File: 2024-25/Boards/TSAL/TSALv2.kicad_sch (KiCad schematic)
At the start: 29 parts, among them J1 043045-0412, Q1 DMP2035U-7, Q3 UJ3N065080K3S, Q4 DMN2056U, U1 H11L1M, U2 NE555D

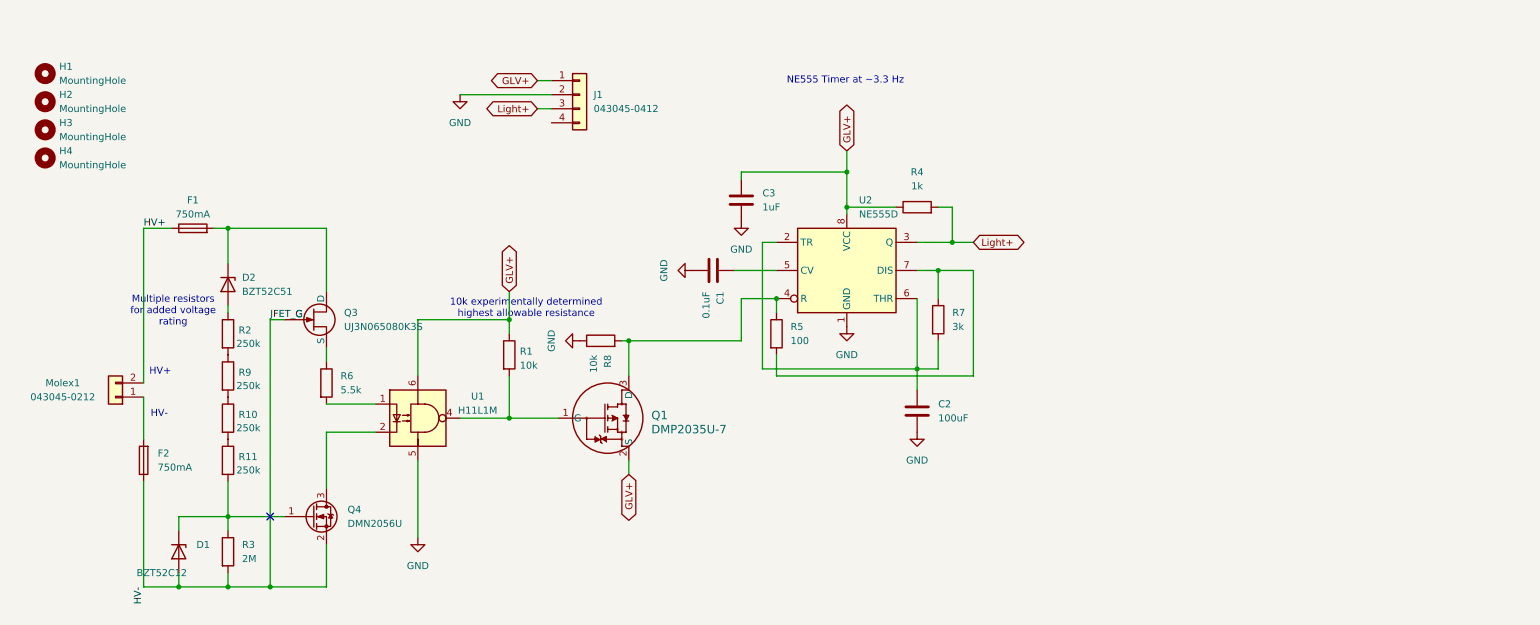
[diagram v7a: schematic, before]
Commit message: fixed up part names and added dnps
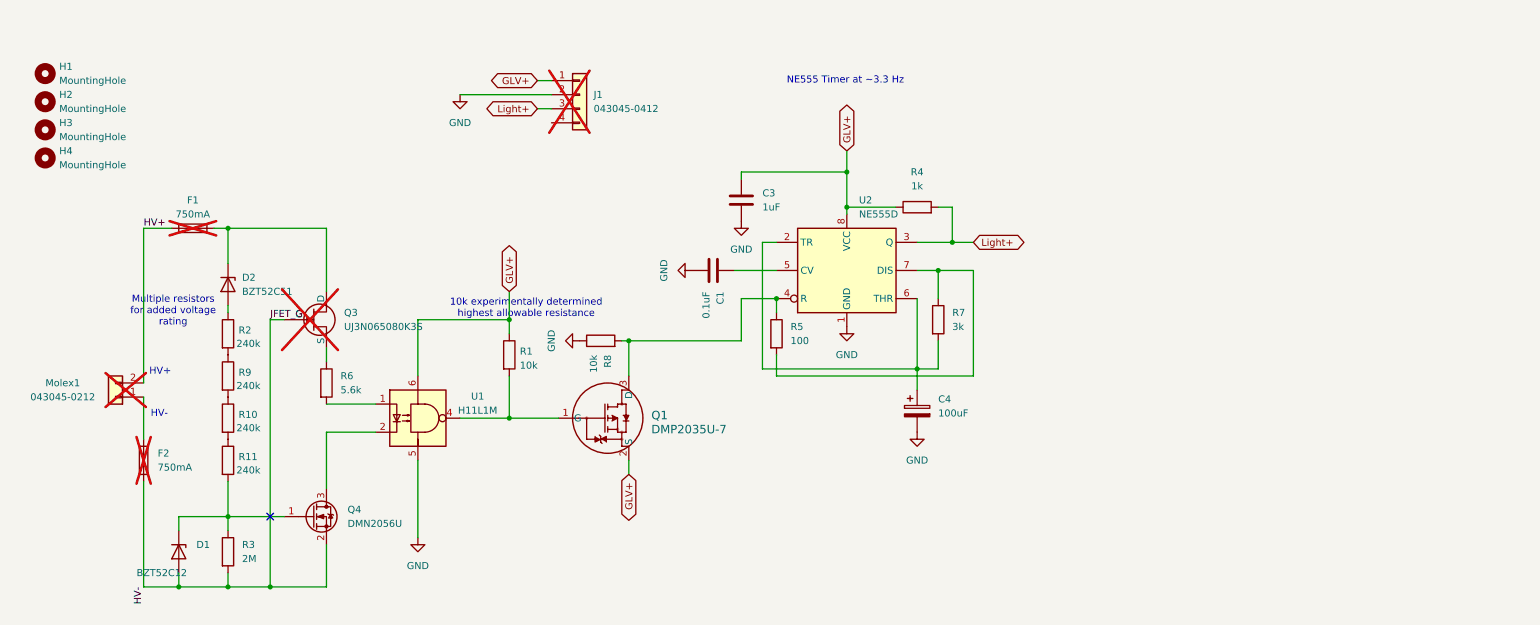
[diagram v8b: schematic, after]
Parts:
- removed C2: 100uF, Capacitor_SMD:C_0805_2012Metric_Pad1.18x1.45mm_HandSolder, symbol Device:C
- added C4: 100uF, Capacitor_SMD:CP_Elec_6.3x5.4, symbol Device:C_Polarized
- F1, F2, J1, Molex1, Q3: now not fitted
- R10, R11, R2, R9: value 250k -> 240k
- R6: value 5.5k -> 5.6k
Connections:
- net GND: now also C4.2
- net at R7.2, U2.2 (TR), U2.6 (THR): now also C4.1
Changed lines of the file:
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@@
 			)
 		)
-		(property "Value" "5.5k"
+		(property "Value" "5.6k"
 			(at 72.39 81.2799 0)
 			(effects
@@
 			)
 		)
-		(property "Value" "250k"
+		(property "Value" "240k"
 			(at 53.594 72.898 0)
 			(effects
@@
 		(in_bom yes)
 		(on_board yes)
-		(dnp no)
+		(dnp yes)
 		(fields_autoplaced yes)
 		(property "Reference" "F1"
@@
 	)
 	(symbol
-		(lib_id "Device:C")
-		(at 176.53 85.09 180)
-		(unit 1)
-		(exclude_from_sim no)
-		(in_bom yes)
-		(on_board yes)
-		(dnp no)
-		(fields_autoplaced yes)
-		(property "Reference" "C2"
-			(at 180.34 83.8199 0)
-			(effects
-				(font
-					(size 1.27 1.27)
-				)
-				(justify right)
-			)
-		)
-		(property "Value" "100uF"
-			(at 180.34 86.3599 0)
-			(effects
-				(font
-					(size 1.27 1.27)
-				)
-				(justify right)
-			)
-		)
-		(property "Footprint" "Capacitor_SMD:C_0805_2012Metric_Pad1.18x1.45mm_HandSolder"
-			(at 175.5648 81.28 0)
-			(effects
-				(font
-					(size 1.27 1.27)
-				)
-				(hide yes)
-			)
-		)
-		(property "Datasheet" "~"
-			(at 176.53 85.09 0)
-			(effects
-				(font
-					(size 1.27 1.27)
-				)
-				(hide yes)
-			)
-		)
-		(property "Description" "Unpolarized capacitor"
-			(at 176.53 85.09 0)
-			(effects
-				(font
-					(size 1.27 1.27)
-				)
-				(hide yes)
-			)
-		)
-		(pin "1"
-		)
-		(pin "2"
-		)
-		(instances
-			(project "TSALv2"
-				(path "/d0262e13-a8ab-42db-962e-1ef7dd9c8d4a"
-					(reference "C2")
-					(unit 1)
-				)
-			)
-		)
-	)
-	(symbol
 		(lib_id "Device:R")
 		(at 52.07 78.74 0)
@@
 			)
 		)
-		(property "Value" "250k"
+		(property "Value" "240k"
 			(at 53.594 80.518 0)
 			(effects
@@
 			)
 		)
-		(property "Value" "250k"
+		(property "Value" "240k"
 			(at 53.594 95.758 0)
 			(effects
@@
 		(in_bom yes)
 		(on_board yes)
-		(dnp no)
+		(dnp yes)
 		(fields_autoplaced yes)
 		(property "Reference" "Q3"
@@
 			)
 		)
-		(property "Value" "250k"
+		(property "Value" "240k"
 			(at 53.594 88.138 0)
 			(effects
@@
 		(in_bom yes)
 		(on_board yes)
-		(dnp no)
+		(dnp yes)
 		(fields_autoplaced yes)
 		(property "Reference" "F2"
@@
 		(in_bom yes)
 		(on_board yes)
-		(dnp no)
+		(dnp yes)
 		(fields_autoplaced yes)
 		(property "Reference" "J1"
@@
 		(in_bom yes)
 		(on_board yes)
-		(dnp no)
+		(dnp yes)
 		(property "Reference" "Molex1"
 			(at 22.225 80.01 0)
@@
 					(unit 1)
 				)
+			)
+		)
+	)
+	(symbol
+		(lib_id "Device:C_Polarized")
+		(at 176.53 85.09 0)
+		(unit 1)
+		(exclude_from_sim no)
+		(in_bom yes)
+		(on_board yes)
+		(dnp no)
+		(fields_autoplaced yes)
+		(property "Reference" "C4"
+			(at 180.34 82.9309 0)
+			(effects
+				(font
+					(size 1.27 1.27)
+				)
+				(justify left)
+			)
+		)
+		(property "Value" "100uF"
+			(at 180.34 85.4709 0)
+			(effects
+				(font
+					(size 1.27 1.27)
+				)
+				(justify left)
+			)
+		)
+		(property "Footprint" "Capacitor_SMD:CP_Elec_6.3x5.4"
+			(at 177.4952 88.9 0)
+			(effects
+				(font
+					(size 1.27 1.27)
+				)
+				(hide yes)
+			)
+		)
+		(property "Datasheet" "~"
+			(at 176.53 85.09 0)
+			(effects
+				(font
+					(size 1.27 1.27)
+				)
+				(hide yes)
+			)
+		)
+		(property "Description" "Polarized capacitor"
+			(at 176.53 85.09 0)
+			(effects
+				(font
+					(size 1.27 1.27)
+				)
+				(hide yes)
+			)
+		)
+		(pin "2"
+		)
+		(pin "1"
+		)
+		(instances
+			(project ""
+				(path "/d0262e13-a8ab-42db-962e-1ef7dd9c8d4a"
+					(reference "C4")
+					(unit 1)
+				)
